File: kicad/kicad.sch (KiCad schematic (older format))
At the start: 51 parts, among them J1 Barrel_Jack_Switch, J2 swim, J3 Conn_01x06, Q1 Q_PMOS_GSD, SW1 SW_Push, U1 RT8097AHGB, U2 STM8L101F3P, U3 RT8097AHGB, U4 PCA9552, U5 ESP-WROOM-02

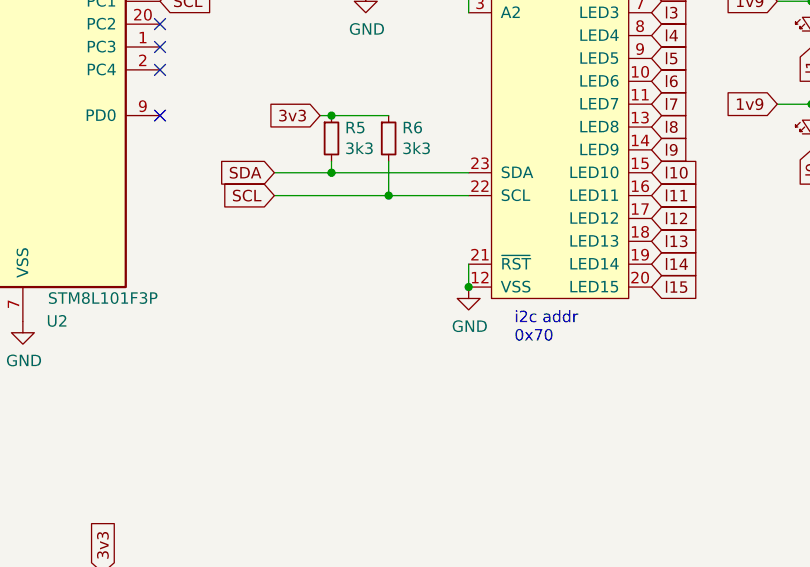
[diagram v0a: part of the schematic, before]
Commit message: Add SW. Update schema with bodge
IT NOW WORKS
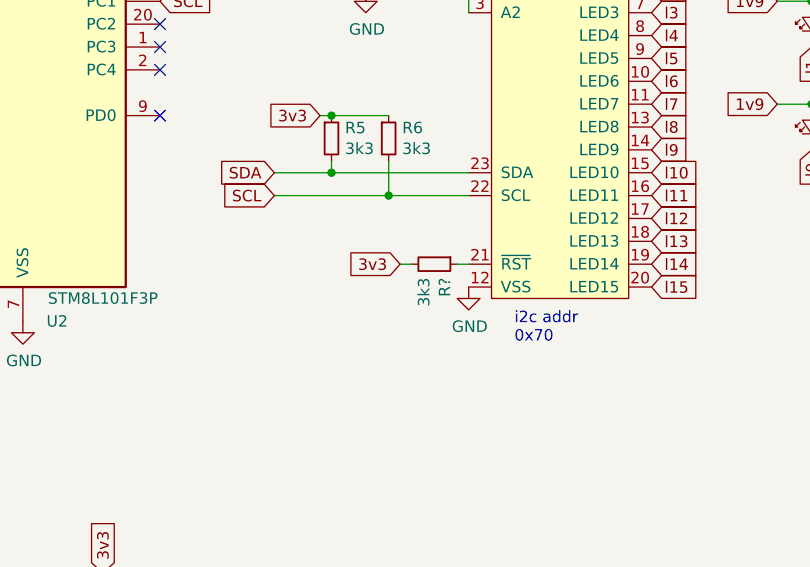
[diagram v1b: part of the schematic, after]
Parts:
- added R?: 3k3, Resistor_SMD:R_0603_1608Metric_Pad1.05x0.95mm_HandSolder, symbol Device:R_Small
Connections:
- net 3v3: now also R?.2
- net GND: no longer U4.21 (~RST)
- new net: R?.1, U4.21 (~RST)
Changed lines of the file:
@@
 	1    0    0    -1
 $EndComp
-Wire Wire Line
-	5650 3900 5650 3800
-Connection ~ 5650 3900
 $Comp
 L Device:R_Small R6
@@
 NoConn ~ 4550 6500
 NoConn ~ 4550 6600
+Text GLabel 5350 3800 0    50   Input ~ 0
+3v3
+$Comp
+L Device:R_Small R?
+U 1 1 60D8E49E
+P 5500 3800
+F 0 "R?" H 5559 3846 50  0000 L CNN
+F 1 "3k3" H 5559 3755 50  0000 L CNN
+F 2 "Resistor_SMD:R_0603_1608Metric_Pad1.05x0.95mm_HandSolder" H 5500 3800 50  0001 C CNN
+F 3 "~" H 5500 3800 50  0001 C CNN
+	1    5500 3800
+	0    1    1    0
+$EndComp
+Wire Wire Line
+	5400 3800 5350 3800
+Wire Wire Line
+	5600 3800 5650 3800
 $EndSCHEMATC
